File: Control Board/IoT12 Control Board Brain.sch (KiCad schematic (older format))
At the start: 36 parts, among them J10 USB_B_Micro, J11 Conn_ARM_JTAG_SWD_10, J9 Conn_ARM_JTAG_SWD_10, SW2 SW_Push, U1 ATSAMD21G18A-AU, U6 AT24C32, Y1 32768Hz

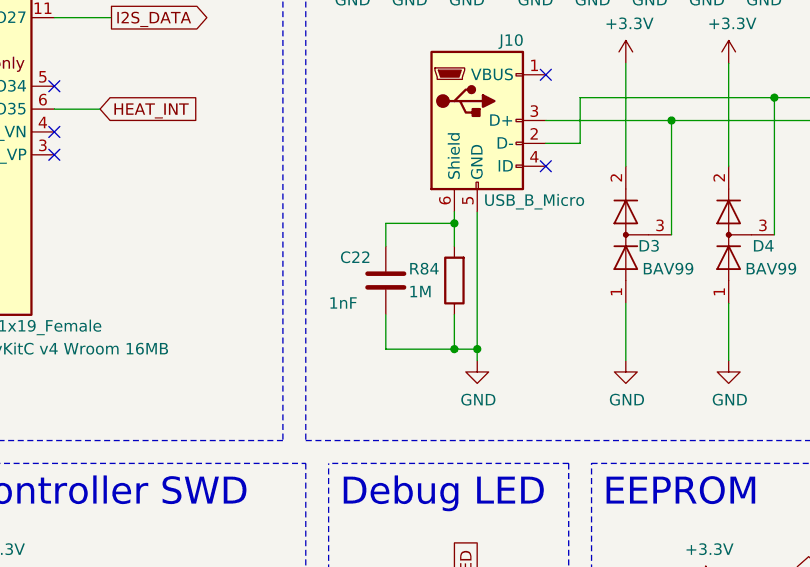
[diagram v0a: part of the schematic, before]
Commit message: Remove capacitor and resistor from usb shield.
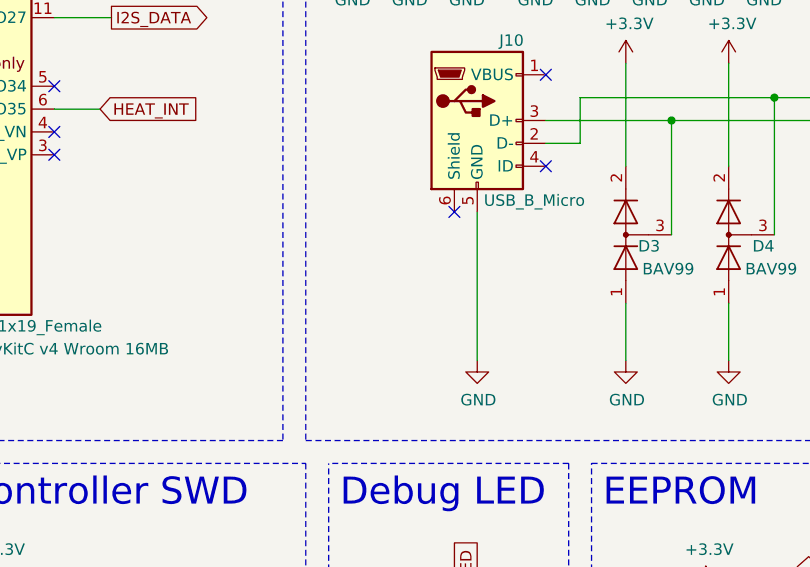
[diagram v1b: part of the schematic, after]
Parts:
- removed C22: 1nF, Capacitor_SMD:C_0805_2012Metric_Pad1.18x1.45mm_HandSolder, symbol Device:C
- removed R84: 1M, Resistor_SMD:R_0805_2012Metric_Pad1.20x1.40mm_HandSolder, symbol Device:R
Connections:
- no-connect marks 32 -> 33
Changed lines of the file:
@@
 Sheet 4 5
 Title "IoT12-hardware brain"
-Date "2021-04-27"
+Date "2021-09-12"
 Rev "V2.1"
 Comp ""
@@
 Text Label 10250 2800 0    50   ~ 0
 D10
-Wire Wire Line
-	5200 4200 5200 4800
-$Comp
-L Device:C C?
-U 1 1 6050233F
-P 4800 4500
-AR Path="/6029EF83/6050233F" Ref="C?"  Part="1"
-AR Path="/60488463/6050233F" Ref="C22"  Part="1"
-F 0 "C22" H 4600 4600 50  0000 L CNN
-F 1 "1nF" H 4550 4400 50  0000 L CNN
-F 2 "Capacitor_SMD:C_0805_2012Metric_Pad1.18x1.45mm_HandSolder" H 4838 4350 50  0001 C CNN
-F 3 "~" H 4800 4500 50  0001 C CNN
-	1    4800 4500
-	1    0    0    -1
-$EndComp
-$Comp
-L Device:R R?
-U 1 1 60502B3B
-P 5100 4500
-AR Path="/604A18A1/60502B3B" Ref="R?"  Part="1"
-AR Path="/60488463/60502B3B" Ref="R84"  Part="1"
-F 0 "R84" H 5300 4450 50  0000 R CNN
-F 1 "1M" H 5300 4550 50  0000 R CNN
-F 2 "Resistor_SMD:R_0805_2012Metric_Pad1.20x1.40mm_HandSolder" V 5030 4500 50  0001 C CNN
-F 3 "~" H 5100 4500 50  0001 C CNN
-	1    5100 4500
-	-1   0    0    1
-$EndComp
-Wire Wire Line
-	5100 4200 5100 4250
-Wire Wire Line
-	5100 4250 4800 4250
-Wire Wire Line
-	4800 4250 4800 4350
-Connection ~ 5100 4250
-Wire Wire Line
-	5100 4250 5100 4350
-Wire Wire Line
-	4800 4650 4800 4800
-Wire Wire Line
-	4800 4800 5100 4800
-Connection ~ 5200 4800
-Wire Wire Line
-	5200 4800 5200 4850
-Wire Wire Line
-	5100 4650 5100 4800
-Connection ~ 5100 4800
-Wire Wire Line
-	5100 4800 5200 4800
 Text Notes 6250 6950 0    50   ~ 0
 I2C: 0x50
@@
 Wire Wire Line
 	1400 1900 1950 1900
+Wire Wire Line
+	5200 4200 5200 4850
+NoConn ~ 5100 4200
 $EndSCHEMATC

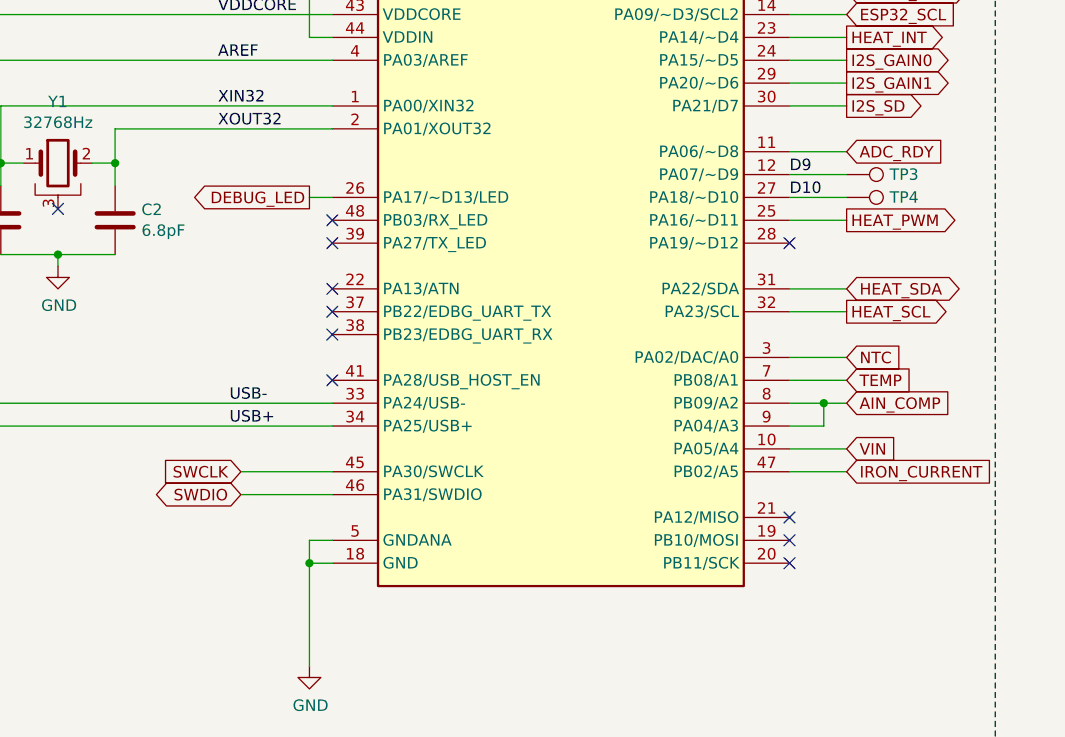
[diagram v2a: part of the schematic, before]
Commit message: Add LCD pin labels. Add testpoints heat controller.
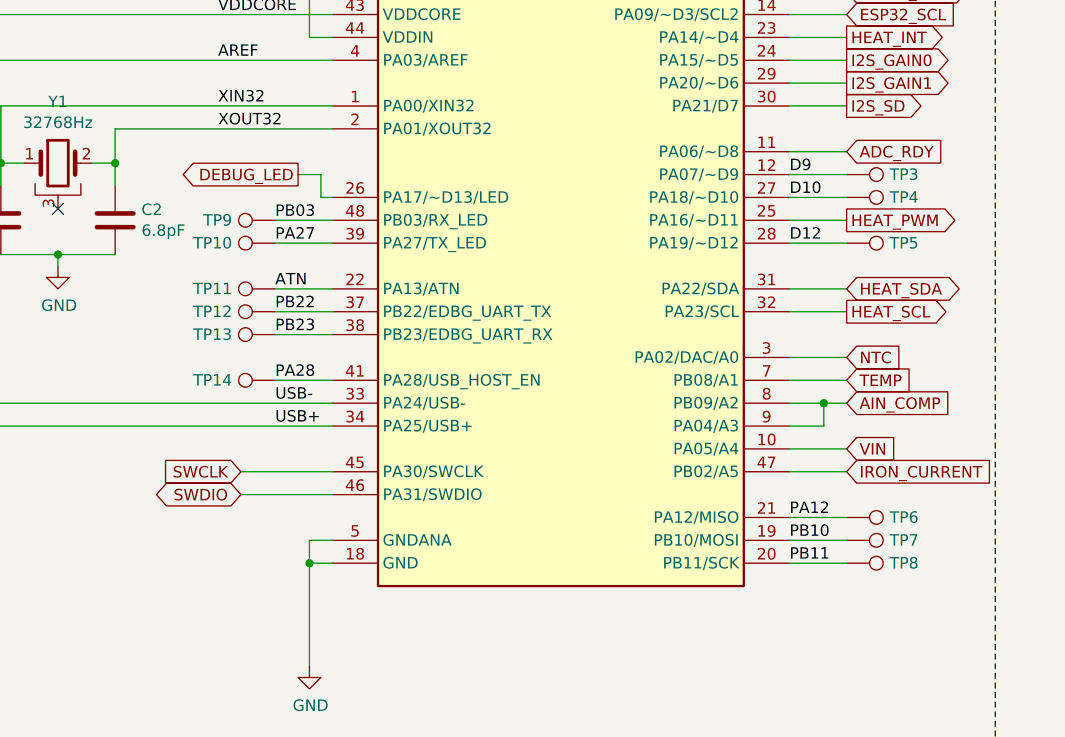
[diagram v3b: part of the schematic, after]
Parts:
- added TP10, TP11, TP12, TP13, TP14, TP5, TP6, TP7, TP8, TP9: TestPoint, TestPoint-extra:TestPoint_Pad_D0.75mm, symbol Connector:TestPoint
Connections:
- net PB10: now reaches U1.19 (PB10/MOSI)
- net PB10: now also TP7.1
- net PB11: now reaches U1.20 (PB11/SCK)
- net PB11: now also TP8.1
- net PA12: now reaches U1.21 (PA12/MISO)
- net PA12: now also TP6.1
- net ATN: now reaches U1.22 (PA13/ATN)
- net ATN: now also TP11.1
- net D12: now reaches U1.28 (PA19/~~D12)
- net D12: now also TP5.1
- net PB22: now reaches U1.37 (PB22/EDBG_UART_TX)
- net PB22: now also TP12.1
- net PB23: now reaches U1.38 (PB23/EDBG_UART_RX)
- net PB23: now also TP13.1
- net PA27: now reaches U1.39 (PA27/TX_LED)
- net PA27: now also TP10.1
- net PA28: now reaches U1.41 (PA28/USB_HOST_EN)
- net PA28: now also TP14.1
- net PB03: now reaches U1.48 (PB03/RX_LED)
- net PB03: now also TP9.1
- no-connect marks 33 -> 23
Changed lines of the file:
@@
 Sheet 4 5
 Title "IoT12-hardware brain"
-Date "2021-09-25"
+Date "2021-09-26"
 Rev "V2.1"
 Comp ""
@@
 Wire Wire Line
 	3350 3750 3550 3750
-$Comp
-L MCU_Microchip_SAMD-extra:SAMD21G_ARDUINO_M0 U1
-U 1 1 60312A43
-P 9250 3000
-F 0 "U1" H 9250 4667 50  0000 C CNN
-F 1 "ATSAMD21G18A-AU" H 9250 4576 50  0000 C CNN
-F 2 "Package_QFP:TQFP-48_7x7mm_P0.5mm" H 9250 2800 50  0001 L CNN
-F 3 "" H 9250 2800 50  0001 L CNN
-	1    9250 3000
-	1    0    0    -1
-$EndComp
 Wire Notes Line
 	4450 550  4450 5200
@@
 Wire Notes Line
 	4550 7700 4550 5300
-Text GLabel 8150 2800 0    50   Output ~ 0
+Text GLabel 8100 2700 0    50   Output ~ 0
 DEBUG_LED
-Wire Wire Line
-	8250 2800 8150 2800
 Text GLabel 5150 6150 1    50   Input ~ 0
 DEBUG_LED
@@
 Wire Wire Line
 	10500 2400 10250 2400
-Text Label 7800 3700 0    50   ~ 0
+Text Label 8000 3700 0    50   ~ 0
 USB-
-Text Label 7800 3800 0    50   ~ 0
+Text Label 8000 3800 0    50   ~ 0
 USB+
 Text Label 7750 1900 0    50   ~ 0
@@
 Wire Wire Line
 	10500 1900 10250 1900
-NoConn ~ 8250 3600
-NoConn ~ 8250 3400
-NoConn ~ 8250 3300
-NoConn ~ 8250 3200
 $Comp
 L Device:C C?
@@
 Wire Wire Line
 	8250 4400 8150 4400
-NoConn ~ 8250 3000
-NoConn ~ 8250 2900
-NoConn ~ 10250 4200
-NoConn ~ 10250 4300
-NoConn ~ 10250 4400
 Wire Wire Line
 	8150 4850 8150 4400
@@
 NoConn ~ 1950 3300
 NoConn ~ 1950 3200
-NoConn ~ 10250 3000
 NoConn ~ 3350 2050
 $Comp
@@
 	5200 4200 5200 4850
 NoConn ~ 5100 4200
+$Comp
+L Connector:TestPoint TP5
+U 1 1 6151C339
+P 10500 3000
+F 0 "TP5" V 10500 3188 50  0000 L CNN
+F 1 "TestPoint" V 10545 3188 50  0001 L CNN
+F 2 "TestPoint-extra:TestPoint_Pad_D0.75mm" H 10700 3000 50  0001 C CNN
+F 3 "~" H 10700 3000 50  0001 C CNN
+	1    10500 3000
+	0    1    1    0
+$EndComp
+Wire Wire Line
+	10250 3000 10500 3000
+$Comp
+L Connector:TestPoint TP6
+U 1 1 6153266E
+P 10500 4200
+F 0 "TP6" V 10500 4388 50  0000 L CNN
+F 1 "TestPoint" V 10545 4388 50  0001 L CNN
+F 2 "TestPoint-extra:TestPoint_Pad_D0.75mm" H 10700 4200 50  0001 C CNN
+F 3 "~" H 10700 4200 50  0001 C CNN
+	1    10500 4200
+	0    1    1    0
+$EndComp
+Wire Wire Line
+	10250 4200 10500 4200
+$Comp
+L MCU_Microchip_SAMD-extra:SAMD21G_ARDUINO_M0 U1
+U 1 1 60312A43
+P 9250 3000
+F 0 "U1" H 9250 4667 50  0000 C CNN
+F 1 "ATSAMD21G18A-AU" H 9250 4576 50  0000 C CNN
+F 2 "Package_QFP:TQFP-48_7x7mm_P0.5mm" H 9250 2800 50  0001 L CNN
+F 3 "" H 9250 2800 50  0001 L CNN
+	1    9250 3000
+	1    0    0    -1
+$EndComp
+$Comp
+L Connector:TestPoint TP7
+U 1 1 6153C7E3
+P 10500 4300
+F 0 "TP7" V 10500 4488 50  0000 L CNN
+F 1 "TestPoint" V 10545 4488 50  0001 L CNN
+F 2 "TestPoint-extra:TestPoint_Pad_D0.75mm" H 10700 4300 50  0001 C CNN
+F 3 "~" H 10700 4300 50  0001 C CNN
+	1    10500 4300
+	0    1    1    0
+$EndComp
+Wire Wire Line
+	10250 4300 10500 4300
+$Comp
+L Connector:TestPoint TP8
+U 1 1 61546341
+P 10500 4400
+F 0 "TP8" V 10500 4588 50  0000 L CNN
+F 1 "TestPoint" V 10545 4588 50  0001 L CNN
+F 2 "TestPoint-extra:TestPoint_Pad_D0.75mm" H 10700 4400 50  0001 C CNN
+F 3 "~" H 10700 4400 50  0001 C CNN
+	1    10500 4400
+	0    1    1    0
+$EndComp
+Wire Wire Line
+	10250 4400 10500 4400
+$Comp
+L Connector:TestPoint TP11
+U 1 1 6155DBA8
+P 8000 3200
+F 0 "TP11" V 8000 3388 50  0000 L CNN
+F 1 "TestPoint" V 8045 3388 50  0001 L CNN
+F 2 "TestPoint-extra:TestPoint_Pad_D0.75mm" H 8200 3200 50  0001 C CNN
+F 3 "~" H 8200 3200 50  0001 C CNN
+	1    8000 3200
+	0    -1   -1   0
+$EndComp
+Wire Wire Line
+	8250 3200 8000 3200
+Text Label 10250 3000 0    50   ~ 0
+D12
+Text Label 10250 4200 0    50   ~ 0
+PA12
+Text Label 10250 4300 0    50   ~ 0
+PB10
+Text Label 10250 4400 0    50   ~ 0
+PB11
+Text Label 8000 3200 0    50   ~ 0
+ATN
+$Comp
+L Connector:TestPoint TP12
+U 1 1 6156F23B
+P 8000 3300
+F 0 "TP12" V 8000 3488 50  0000 L CNN
+F 1 "TestPoint" V 8045 3488 50  0001 L CNN
+F 2 "TestPoint-extra:TestPoint_Pad_D0.75mm" H 8200 3300 50  0001 C CNN
+F 3 "~" H 8200 3300 50  0001 C CNN
+	1    8000 3300
+	0    -1   -1   0
+$EndComp
+Wire Wire Line
+	8250 3300 8000 3300
+Text Label 8000 3300 0    50   ~ 0
+PB22
+$Comp
+L Connector:TestPoint TP13
+U 1 1 615794EF
+P 8000 3400
+F 0 "TP13" V 8000 3588 50  0000 L CNN
+F 1 "TestPoint" V 8045 3588 50  0001 L CNN
+F 2 "TestPoint-extra:TestPoint_Pad_D0.75mm" H 8200 3400 50  0001 C CNN
+F 3 "~" H 8200 3400 50  0001 C CNN
+	1    8000 3400
+	0    -1   -1   0
+$EndComp
+Wire Wire Line
+	8250 3400 8000 3400
+Text Label 8000 3400 0    50   ~ 0
+PB23
+$Comp
+L Connector:TestPoint TP10
+U 1 1 6158D44B
+P 8000 3000
+F 0 "TP10" V 8000 3188 50  0000 L CNN
+F 1 "TestPoint" V 8045 3188 50  0001 L CNN
+F 2 "TestPoint-extra:TestPoint_Pad_D0.75mm" H 8200 3000 50  0001 C CNN
+F 3 "~" H 8200 3000 50  0001 C CNN
+	1    8000 3000
+	0    -1   -1   0
+$EndComp
+Wire Wire Line
+	8250 3000 8000 3000
+Text Label 8000 3000 0    50   ~ 0
+PA27
+$Comp
+L Connector:TestPoint TP14
+U 1 1 615A6F09
+P 8000 3600
+F 0 "TP14" V 8000 3788 50  0000 L CNN
+F 1 "TestPoint" V 8045 3788 50  0001 L CNN
+F 2 "TestPoint-extra:TestPoint_Pad_D0.75mm" H 8200 3600 50  0001 C CNN
+F 3 "~" H 8200 3600 50  0001 C CNN
+	1    8000 3600
+	0    -1   -1   0
+$EndComp
+Wire Wire Line
+	8250 3600 8000 3600
+Text Label 8000 3600 0    50   ~ 0
+PA28
+$Comp
+L Connector:TestPoint TP9
+U 1 1 615B433E
+P 8000 2900
+F 0 "TP9" V 8000 3088 50  0000 L CNN
+F 1 "TestPoint" V 8045 3088 50  0001 L CNN
+F 2 "TestPoint-extra:TestPoint_Pad_D0.75mm" H 8200 2900 50  0001 C CNN
+F 3 "~" H 8200 2900 50  0001 C CNN
+	1    8000 2900
+	0    -1   -1   0
+$EndComp
+Wire Wire Line
+	8250 2900 8000 2900
+Text Label 8000 2900 0    50   ~ 0
+PB03
+Wire Wire Line
+	8250 2800 8200 2800
+Wire Wire Line
+	8200 2800 8200 2700
+Wire Wire Line
+	8200 2700 8100 2700
 $EndSCHEMATC
